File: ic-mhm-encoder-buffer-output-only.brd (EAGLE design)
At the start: 68 x 58.3 mm, 35 parts, among them IC1 LS7183-SOIC, J1 2023960907, J2 2023960607, M1 BSS670S2LH6327XTSA1, SW1 CS-4-13NTA, U1 24LC16BT-I/MC, U2 D5V0F4U6S-7, U3 D5V0F4U6S-7, U4 D5V0F4U6S-7

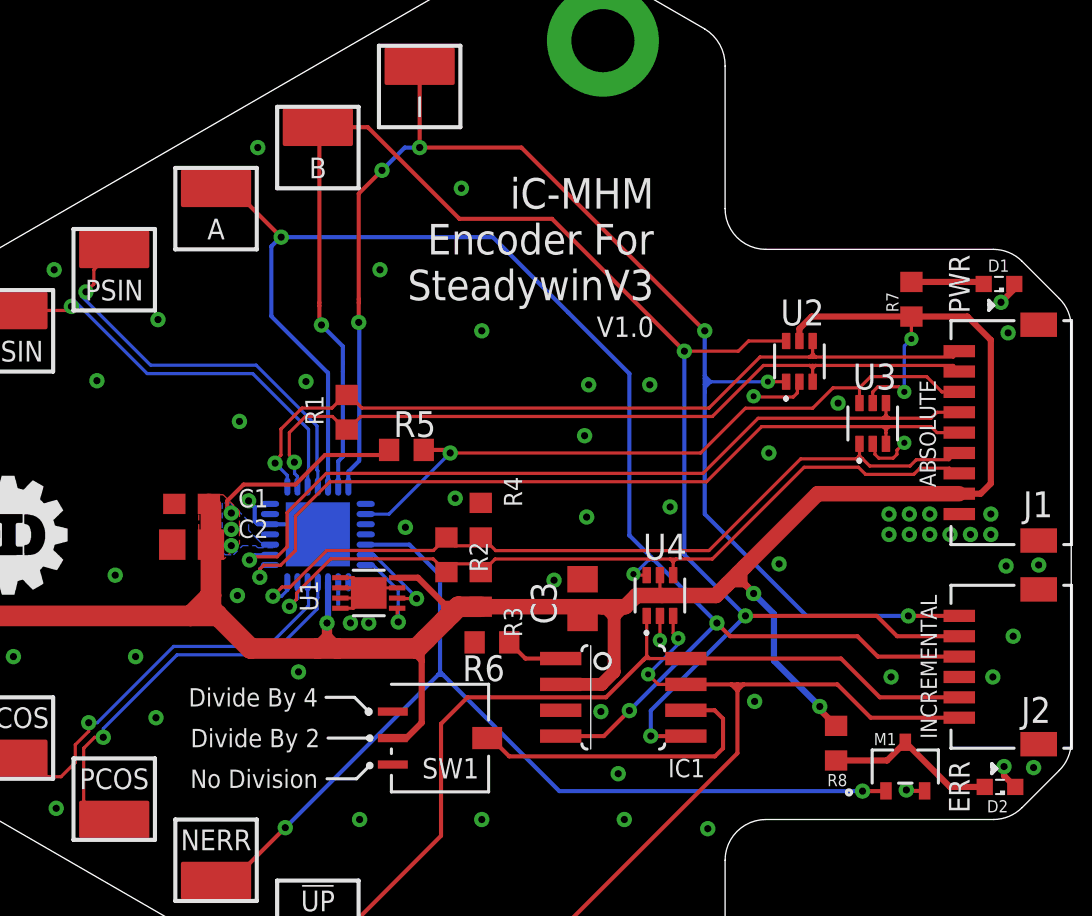
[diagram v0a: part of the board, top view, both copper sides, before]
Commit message: added verisons with buffers on ABI
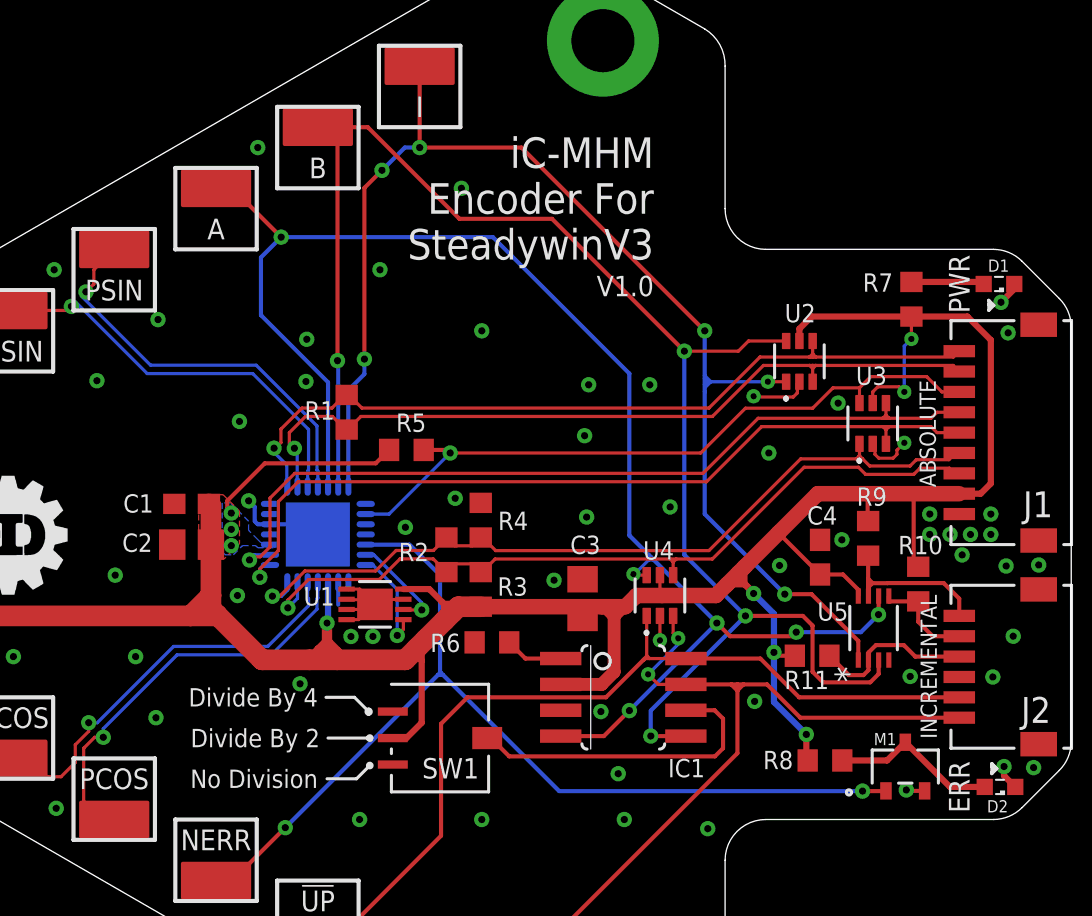
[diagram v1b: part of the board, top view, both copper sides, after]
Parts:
- added C4: 0.1uF, rcl:C0603
- added R10, R11, R9: 10K, rcl:R0603
- added U5: SN74LVC3G07QDCURQ1, ic-mhm:DCU8_TEX
- moved R8 1.01 mm to (24.9, -11.1), turned to 0 degrees
- moved U1 0.64 mm to (2.80, -3.43)
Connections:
- new net ENC_A_OUT: J2.4, R11.2, U5.2
- new net ENC_B_OUT: J2.5, R10.2, U5.5
- new net ENC_Z_OUT: J2.6, R9.2, U5.7
- net ENC_A: now also U5.6; no longer J2.4
- net ENC_B: now also U5.3; no longer J2.5
- net ENC_Z: now also U5.1; no longer J2.6
- net GND: now also C4.2, U5.4
- net VDD: now also C4.1, R10.1, R11.1, R9.1, U5.8
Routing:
- net VDD: track 142.3 -> 155.8 mm, vias 8 -> 9
- net ENC_Z_OUT: track 0.00 -> 9.11 mm
- net ENC_A_OUT: track 0.00 -> 8.12 mm
- net ENC_B_OUT: track 0.00 -> 5.01 mm
- net ENC_Z: track 69.2 -> 65.6 mm
- net ENC_A: track 76.7 -> 74.0 mm, vias 4 -> 6
- net GND: track 23.6 -> 25.3 mm, vias 70 -> 69
- net ENC_B: track 80.7 -> 79.3 mm
- net SDA: track 4.37 -> 5.21 mm
- net SCL: track 4.38 -> 5.00 mm
- added copper zone on layer 15, net NOT_GND
- added copper zone on layer 2, net NOT_GND
